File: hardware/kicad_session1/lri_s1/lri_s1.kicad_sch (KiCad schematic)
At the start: 47 parts, among them J1 USB_C_Receptacle_USB2.0_16P, J2 PY1, J3 PY1, Q1 NMOS, Q2 NMOS, Q3 CSD17318Q2, SW1 MJTP1230, SW2 MJTP1230, U1 STM32F042F6P6, U2 LP5912-3.3DRV, U3 ICM-20602, U4 BMP280

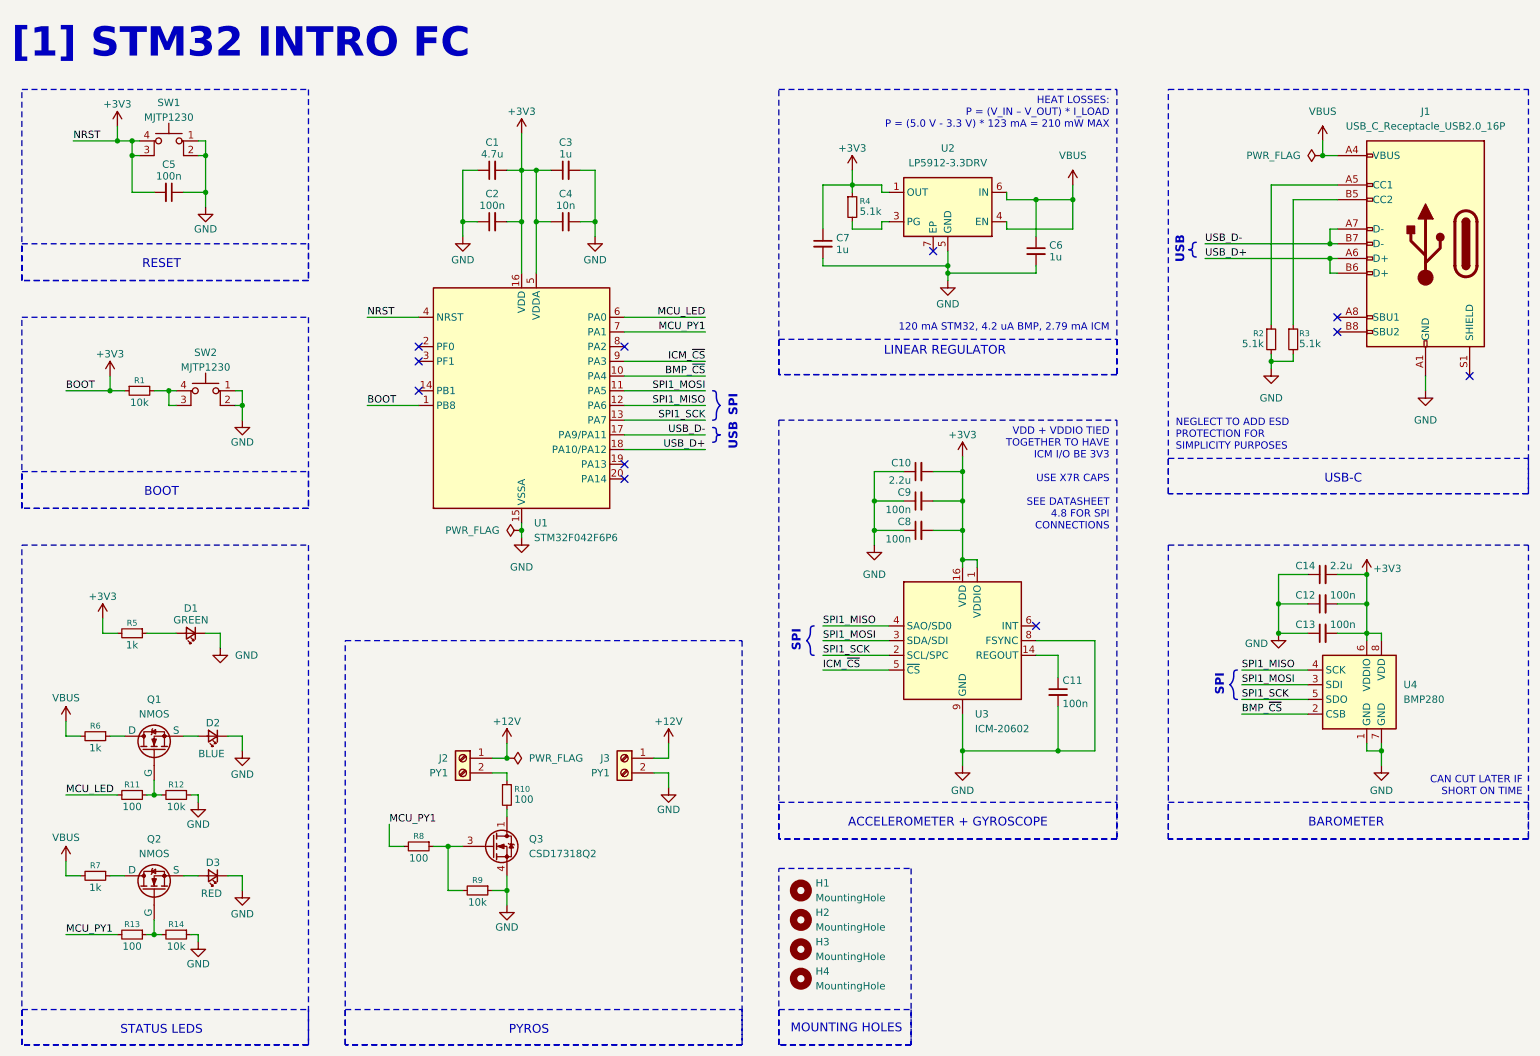
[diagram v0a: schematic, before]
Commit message: Changed components to non-obsolete versions, IMU + barometer. Added SD card for data-logging. Removed pyros. Added servo connectors.
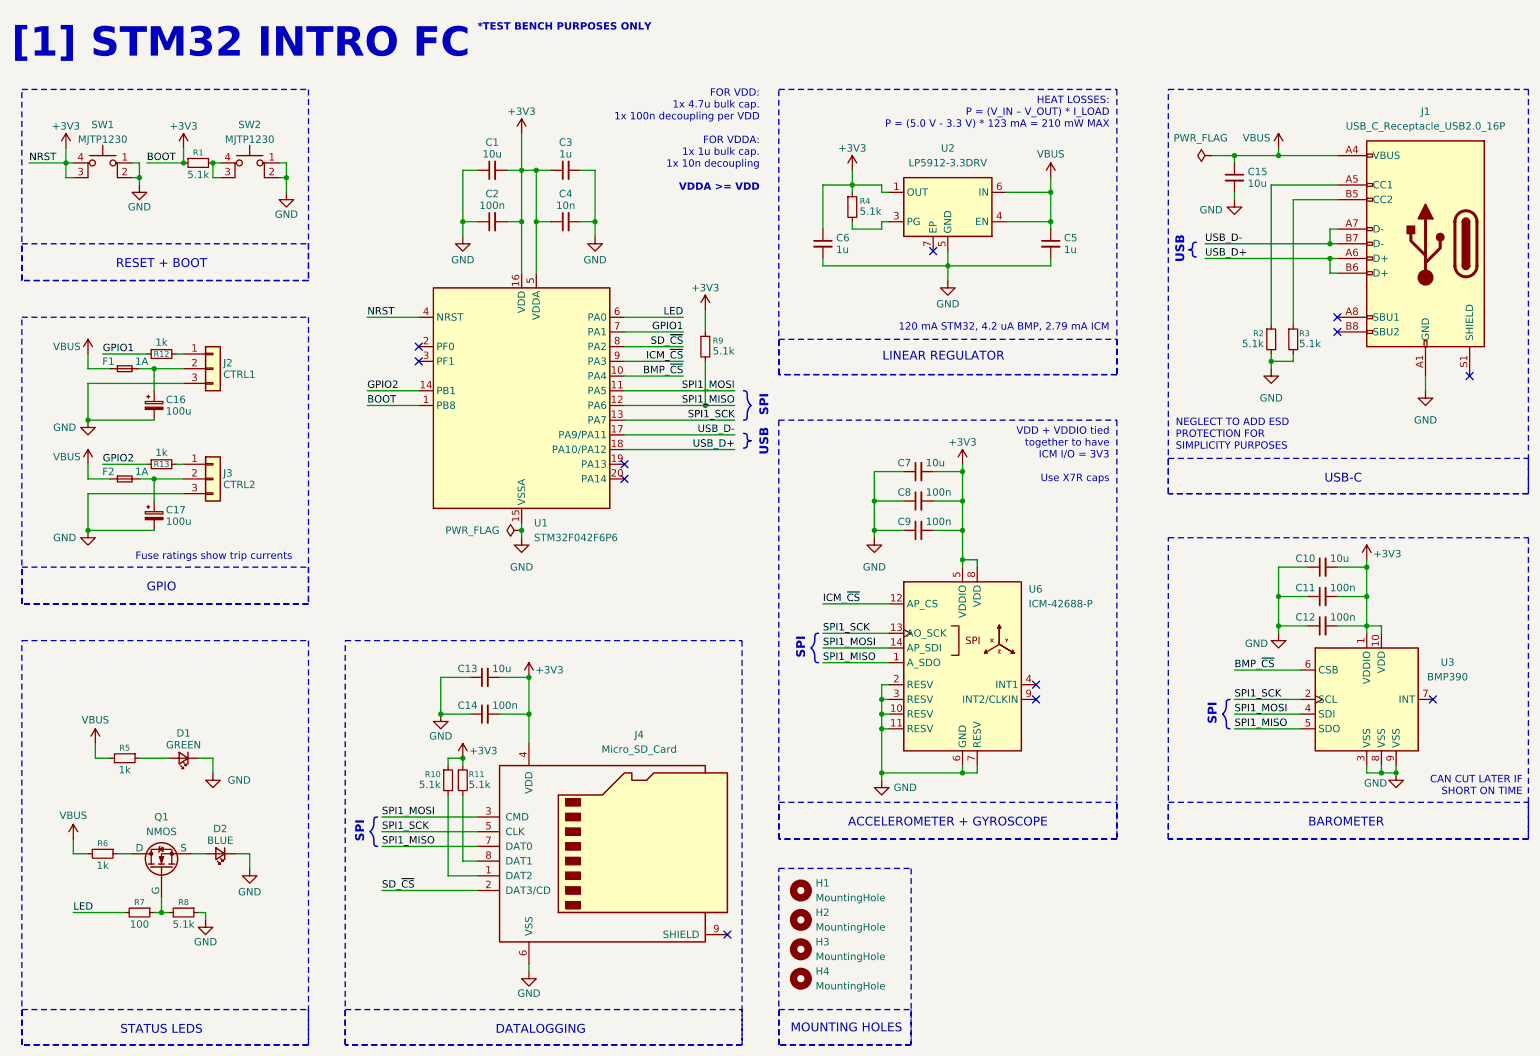
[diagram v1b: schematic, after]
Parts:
- removed C11, C5: 100n, symbol Device:C_Small
- removed D3: RED, symbol Device:LED_Small
- removed J2, J3: PY1, symbol Connector:Screw_Terminal_01x02
- removed Q2: NMOS, symbol Simulation_SPICE:NMOS
- removed Q3: CSD17318Q2, Package_SON:Texas_DQK, symbol Transistor_FET:CSD17313Q2
- removed R14: 10k, symbol Device:R_Small
- removed R7: 1k, symbol Device:R_Small
- removed R8: 100, symbol Device:R_Small
- removed U3: ICM-20602, Package_LGA:LGA-16_3x3mm_P0.5mm_LayoutBorder3x5y, symbol Sensor_Motion:ICM-20602
- removed U4: BMP280, Package_LGA:Bosch_LGA-8_2x2.5mm_P0.65mm_ClockwisePinNumbering, symbol Sensor_Pressure:BMP280
- added C13, C15: 10u, Capacitor_SMD:C_0402_1005Metric, symbol Device:C_Small
- added C14: 100n, Capacitor_SMD:C_0402_1005Metric, symbol Device:C_Small
- added C16, C17: 100u, symbol Device:C_Polarized_Small
- added F1, F2: 1A, symbol Device:Fuse_Small
- added J2: CTRL1, symbol Connector_Generic:Conn_01x03
- added J3: CTRL2, symbol Connector_Generic:Conn_01x03
- added J4: Micro_SD_Card, symbol Connector:Micro_SD_Card
- added R11: 5.1k, Resistor_SMD:R_0402_1005Metric, symbol Device:R_Small
- added R12: 1k, Resistor_SMD:R_0201_0603Metric, symbol Device:R_Small
- added U3: BMP390, symbol lri_s1_symbols:BMP390
- added U6: ICM-42688-P, symbol lri_s1_symbols:ICM-42688-P
- C1: value 4.7u -> 10u; footprint (none) -> Capacitor_SMD:C_0603_1608Metric
- C10: renamed from C14; value 2.2u -> 10u; footprint (none) -> Capacitor_SMD:C_0402_1005Metric
- C11: renamed from C12; footprint (none) -> Capacitor_SMD:C_0402_1005Metric
- C12: renamed from C13; footprint (none) -> Capacitor_SMD:C_0402_1005Metric
- C2, C3, C4: footprint (none) -> Capacitor_SMD:C_0402_1005Metric
- C5: renamed from C6; footprint (none) -> Capacitor_SMD:C_0402_1005Metric
- C6: renamed from C7; footprint (none) -> Capacitor_SMD:C_0402_1005Metric
- C7: renamed from C10; value 2.2u -> 10u; footprint (none) -> Capacitor_SMD:C_0402_1005Metric
- C8: renamed from C9; footprint (none) -> Capacitor_SMD:C_0402_1005Metric
- C9: renamed from C8; footprint (none) -> Capacitor_SMD:C_0402_1005Metric
- D1, D2: footprint (none) -> LED_SMD:LED_0402_1005Metric
- H1, H2, H3, H4: footprint (none) -> MountingHole:MountingHole_3.2mm_M3
- J1: footprint (none) -> Connector_USB:USB_C_Receptacle_GCT_USB4110
- R1: value 10k -> 5.1k; footprint (none) -> Resistor_SMD:R_0201_0603Metric
- R10: value 100 -> 5.1k; footprint (none) -> Resistor_SMD:R_0402_1005Metric
- R13: value 100 -> 1k; footprint (none) -> Resistor_SMD:R_0201_0603Metric
- R2, R3, R4, R5, R6: footprint (none) -> Resistor_SMD:R_0402_1005Metric
- R7: renamed from R11; footprint (none) -> Resistor_SMD:R_0402_1005Metric
- R8: renamed from R12; value 10k -> 5.1k; footprint (none) -> Resistor_SMD:R_0201_0603Metric
- R9: value 10k -> 5.1k; footprint (none) -> Resistor_SMD:R_0402_1005Metric
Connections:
- net +3V3: now also R10.1, R9.1, C13.2, C14.2, J4.4 (VDD), R11.1, U3.1 (VDDIO), U3.10 (VDD), U6.5 (VDDIO), U6.8 (VDD); no longer R5.2
- net BMP_~{CS}: now also U3.6 (CSB)
- net GND: now also C13.1, C14.1, C15.2, C16.2, C17.2, J2.3 (Pin_3), J3.3 (Pin_3), J4.6 (VSS), U3.3 (VSS), U3.8 (VSS), U3.9 (VSS), U6.10 (RESV), U6.11 (RESV), U6.2 (RESV), U6.3 (RESV), U6.6 (GND), U6.7 (RESV); no longer R9.1
- net ICM_~{CS}: now also U6.12 (AP_CS)
- net SPI1_MISO: now also R9.2, J4.7 (DAT0), U3.5 (SDO), U6.1 (A_SDO)
- net SPI1_MOSI: now also J4.3 (CMD), U3.4 (SDI), U6.14 (AP_SDI)
- net SPI1_SCK: now also J4.5 (CLK), U3.2 (SCL), U6.13 (AO_SCK)
- net VBUS: now also R5.2, C15.1, F1.1, F2.1
- net at R10.2: now also J4.1 (DAT2)
- net GPIO2: now reaches R13.1
- net GPIO2: now also U1.14 (PB1)
- net SD_~{CS}: now reaches U1.8 (PA2)
- net SD_~{CS}: now also J4.2 (DAT3/CD)
- net MCU_LED renamed LED
- net MCU_PY1: no longer names the net of R13.2
- net MCU_PY1: now also J3.1 (Pin_1); no longer U1.7 (PA1)
- new net: C16.1, F1.2, J2.2 (Pin_2)
- new net: C17.1, F2.2, J3.2 (Pin_2)
- new net: J2.1 (Pin_1), R12.2
- new net: J4.8 (DAT1), R11.2
- new net GPIO1: R12.1, U1.7 (PA1)
- no-connect marks 11 -> 12
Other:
- note added: "*TEST BENCH PURPOSES ONLY"
- note added: "DATALOGGING"
- note added: "FOR VDD: 1x 4.7u bulk cap. 1x 100n decoupling per VDD FOR VDDA: 1x 1u bulk cap. 1x 10n decoupling"
- note added: "Fuse ratings show trip currents"
- note added: "GPIO"
- note added: "RESET + BOOT"
- note added: "VDD + VDDIO tied together to have ICM I/O = 3V3 Use X7R caps"
- note added: "VDDA >= VDD"
- note removed: "BOOT"
- note removed: "PYROS"
- note removed: "RESET"
- note removed: "VDD + VDDIO TIED TOGETHER TO HAVE ICM I/O BE 3V3 USE X7R CAPS SEE DATASHEET 4.8 FOR SPI CONNECTIONS"
- moved on the sheet: C10, C11, C12, C5, D1, D2, Q1, R1, R5, R6, R7, R8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
